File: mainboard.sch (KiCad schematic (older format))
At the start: 23 parts, among them J13 Barrel_Jack, J14 USB_A, J15 Conn_01x03_Male, J16 Conn_01x03_Male, J17 Conn_01x03_Male, J18 Conn_01x03_Male, J19 Conn_01x03_Male, J20 Conn_01x03_Male, J21 Conn_01x03_Male, J22 Conn_01x12_Female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

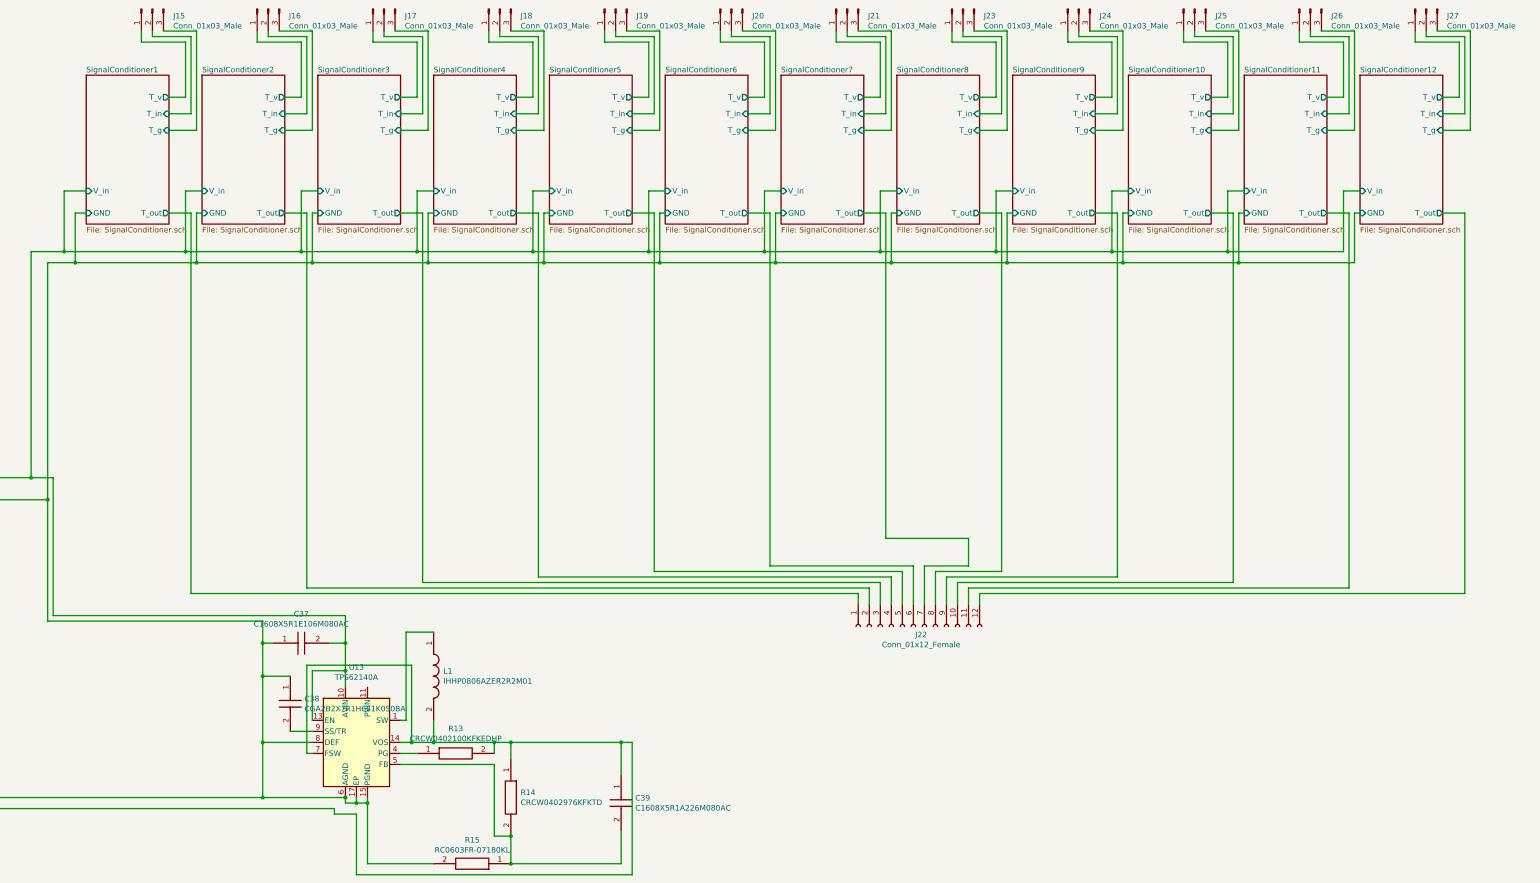
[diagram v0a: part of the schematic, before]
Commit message: Updated Parts
Updated parts to components that are available for order rather than obsolete, out-of-stock, or non-real components.
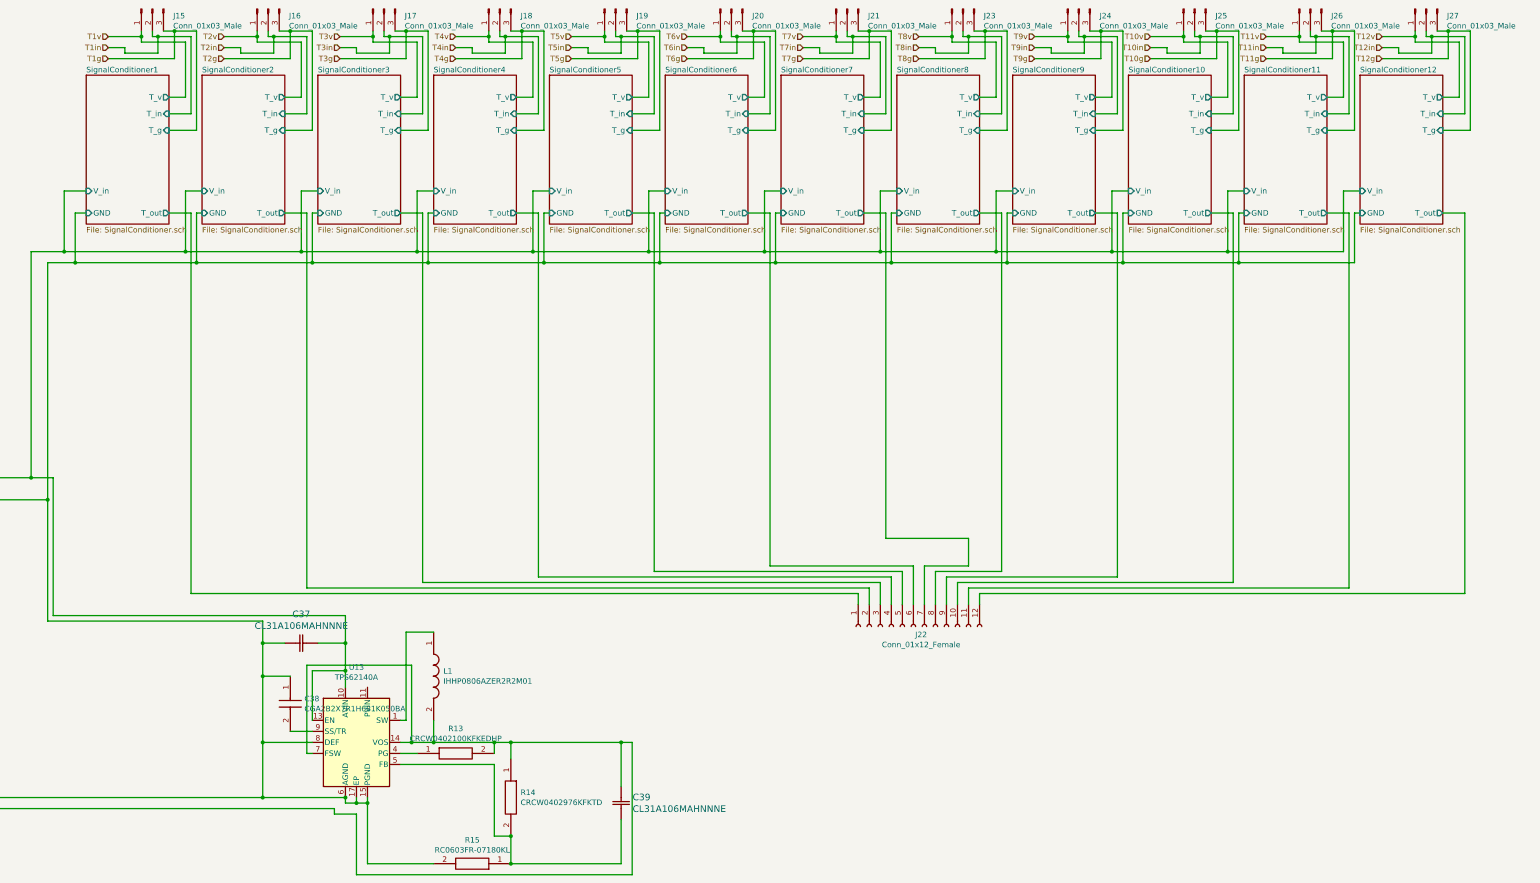
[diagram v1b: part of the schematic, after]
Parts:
- removed C37: C1608X5R1E106M080AC, CAPC1608X80N, symbol SamacSys_Parts:C1608X5R1E106M080AC
- removed C39: C1608X5R1A226M080AC, CAPC1608X80N, symbol SamacSys_Parts:C1608X5R1A226M080AC
- added C37, C39: CL31A106MAHNNNE, CAP_CL31_SAM, symbol CL31A106MAHNNNE:CL31A106MAHNNNE
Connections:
- net 0: now also C37.1
- net 5.1Vout: now also C39.1
- net SignalConditioner1/V_in: now also C37.2
- net at R14.2, R15.1, U13.5 (FB): now also C39.2
- net SignalConditioner1/T_g renamed T1g
- net SignalConditioner1/T_in renamed T1in
- net SignalConditioner1/T_v renamed T1v
- net SignalConditioner10/T_g renamed T10g
- net SignalConditioner10/T_in renamed T10in
- net SignalConditioner10/T_v renamed T10v
- net SignalConditioner11/T_g renamed T11g
- net SignalConditioner11/T_in renamed T11in
- net SignalConditioner11/T_v renamed T11v
- net SignalConditioner12/T_g renamed T12g
- net SignalConditioner12/T_in renamed T12in
- net SignalConditioner12/T_v renamed T12v
- net SignalConditioner2/T_g renamed T2g
- net SignalConditioner2/T_in renamed T2in
- net SignalConditioner2/T_v renamed T2v
- net SignalConditioner3/T_g renamed T3g
- net SignalConditioner3/T_in renamed T3in
- net SignalConditioner3/T_v renamed T3v
- net SignalConditioner4/T_g renamed T4g
- net SignalConditioner4/T_in renamed T4in
- net SignalConditioner4/T_v renamed T4v
- net SignalConditioner5/T_g renamed T5g
- net SignalConditioner5/T_in renamed T5in
- net SignalConditioner5/T_v renamed T5v
- net SignalConditioner6/T_g renamed T6g
- net SignalConditioner6/T_in renamed T6in
- net SignalConditioner6/T_v renamed T6v
- net SignalConditioner7/T_g renamed T7g
- net SignalConditioner7/T_in renamed T7in
- net SignalConditioner7/T_v renamed T7v
- net SignalConditioner8/T_g renamed T8g
- net SignalConditioner8/T_in renamed T8in
- net SignalConditioner8/T_v renamed T8v
- net SignalConditioner9/T_g renamed T9g
- net SignalConditioner9/T_in renamed T9in
- net SignalConditioner9/T_v renamed T9v

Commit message: Finished Component Selection
Finished Component selection in schematic and BoM. Ready to design PCB
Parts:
- removed J13: Barrel_Jack, symbol Connector:Barrel_Jack
- removed J14: USB_A, symbol Connector:USB_A
- removed J15, J16, J17, J18, J19, J20, J21, J23, J24, J25, J26, J27: Conn_01x03_Male, symbol Connector:Conn_01x03_Male
- removed J22: Conn_01x12_Female, symbol Connector:Conn_01x12_Female
- added J13: SS-52100-001, CONN15_2100-001_STW, symbol SS-52100-001:SS-52100-001
- added J14: PJ-102A, PJ-102A_CUD, symbol PJ-102A:PJ-102A
- added J15, J16, J17, J18, J19, J20, J21, J23, J24, J25, J26, J27: 644752-3, 644752-3_TYC, symbol 644752-3:644752-3
- added J22: PPTC121LFBN-RC, Conn12_1p2x0p1_SUL, symbol PPTC121LFBN-RC:PPTC121LFBN-RC
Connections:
- net SignalConditioner1/V_in is gone; now on net 9Vin: C37.2, U13.10 (AVIN), U13.13 (EN)
- net 0: now also J13.4, J14.2
- net 5.1Vout: now also J13.1
- net 9Vin: now also J14.1
- net SignalConditioner1/T_out: now also J22.1
- net SignalConditioner10/T_out: now also J22.10
- net SignalConditioner11/T_out: now also J22.11
- net SignalConditioner12/T_out: now also J22.12
- net SignalConditioner2/T_out: now also J22.2
- net SignalConditioner3/T_out: now also J22.3
- net SignalConditioner4/T_out: now also J22.4
- net SignalConditioner5/T_out: now also J22.5
- net SignalConditioner6/T_out: now also J22.6
- net SignalConditioner7/T_out: now also J22.7
- net SignalConditioner8/T_out: now also J22.8
- net SignalConditioner9/T_out: now also J22.9
- net T10g: now also J25.3 (Pin_3)
- net T10in: now also J25.2 (Pin_2)
- net T10v: now also J25.1 (Pin_1)
- net T11g: now also J26.3 (Pin_3)
- net T11in: now also J26.2 (Pin_2)
- net T11v: now also J26.1 (Pin_1)
- net T12g: now also J27.3 (Pin_3)
- net T12in: now also J27.2 (Pin_2)
- net T12v: now also J27.1 (Pin_1)
- net T1g: now also J15.3 (Pin_3)
- net T1in: now also J15.2 (Pin_2)
- net T1v: now also J15.1 (Pin_1)
- net T2g: now also J16.3 (Pin_3)
- net T2in: now also J16.2 (Pin_2)
- net T2v: now also J16.1 (Pin_1)
- net T3g: now also J17.3 (Pin_3)
- net T3in: now also J17.2 (Pin_2)
- net T3v: now also J17.1 (Pin_1)
- net T4g: now also J18.3 (Pin_3)
- net T4in: now also J18.2 (Pin_2)
- net T4v: now also J18.1 (Pin_1)
- net T5g: now also J19.3 (Pin_3)
- net T5in: now also J19.2 (Pin_2)
- net T5v: now also J19.1 (Pin_1)
- net T6g: now also J20.3 (Pin_3)
- net T6in: now also J20.2 (Pin_2)
- net T6v: now also J20.1 (Pin_1)
- net T7g: now also J21.3 (Pin_3)
- net T7in: now also J21.2 (Pin_2)
- net T7v: now also J21.1 (Pin_1)
- net T8g: now also J23.3 (Pin_3)
- net T8in: now also J23.2 (Pin_2)
- net T8v: now also J23.1 (Pin_1)
- net T9g: now also J24.3 (Pin_3)
- net T9in: now also J24.2 (Pin_2)
- net T9v: now also J24.1 (Pin_1)
- no-connect marks 0 -> 3
